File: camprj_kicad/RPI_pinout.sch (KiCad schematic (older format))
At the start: 1 part, among them J1 ESQ-120-69-G-D-LL

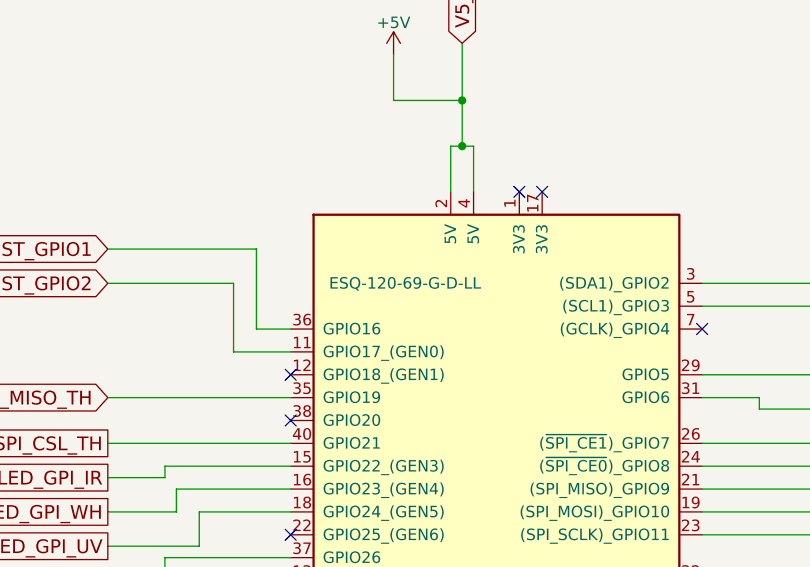
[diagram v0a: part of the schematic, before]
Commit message: Board design: component placement done
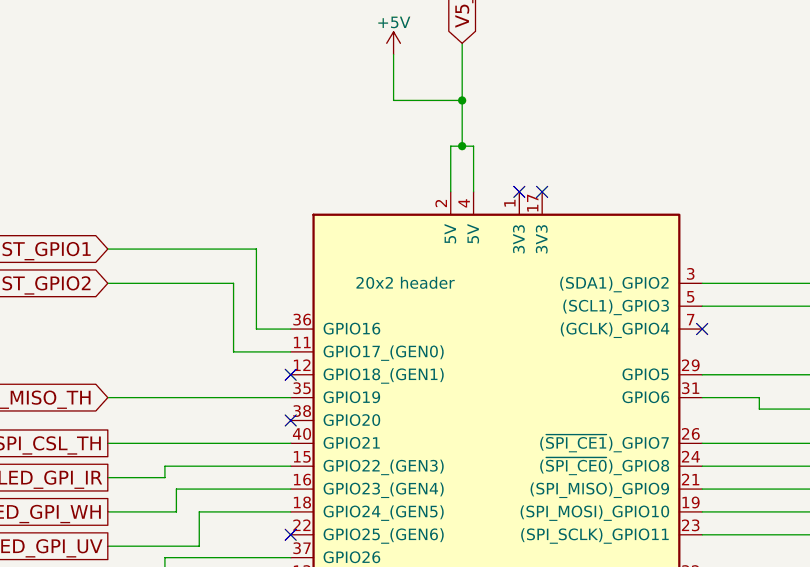
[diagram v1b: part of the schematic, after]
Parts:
- J1: value ESQ-120-69-G-D-LL -> 20x2 header
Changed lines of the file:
@@
 EESchema Schematic File Version 2
+LIBS:camprj_kicad-rescue
 LIBS:power
 LIBS:device
@@
 P 3950 3250
 F 0 "J1" H 4650 2000 50  0000 C CNN
-F 1 "ESQ-120-69-G-D-LL" H 3550 4150 50  0000 C CNN
+F 1 "20x2 header" H 3550 4150 50  0000 C CNN
 F 2 "Pin_Headers:Pin_Header_Straight_2x20_Pitch2.54mm" H 4950 4500 50  0001 C CNN
 F 3 "http://suddendocs.samtec.com/catalog_english/esq_th.pdf" H 4000 3100 50  0001 C CNN

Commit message: Final Delivery
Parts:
- J1: MPN (none) -> ESQ-120-69-G-D-LL
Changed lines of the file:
@@
 Date "2017-07-06"
 Rev "1"
-Comp "D-HEST ETH Zurich"
+Comp "MHSL ETH Zurich"
 Comment1 "Geethan Karunaratne"
 Comment2 ""
@@
 F 3 "http://suddendocs.samtec.com/catalog_english/esq_th.pdf" H 4000 3100 50  0001 C CNN
 F 4 "https://www.digikey.com/product-detail/en/ESQ-120-69-G-D-LL/ESQ-120-69-G-D-LL-ND/7098805?WT.z_cid=ref_neda_dkc_buynow" H 3950 3250 60  0001 C CNN "Buy Link"
+F 5 "ESQ-120-69-G-D-LL" H 3950 3250 60  0001 C CNN "MPN"
 	1    3950 3250
 	1    0    0    -1
